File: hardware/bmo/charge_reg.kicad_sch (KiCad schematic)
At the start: 19 parts, among them U1 BQ25606RGET, U4 TPS61088RHLR

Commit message: wip start ltc4412 addition
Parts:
- added U5: LTC4412xS6, Package_TO_SOT_SMD:TSOT-23-6, symbol Power_Management:LTC4412xS6
- added U6, U7: SIA445EDJ-T1-GE3, Package_TO_SOT_SMD:Vishay_PowerPAK_SC70-6L_Single, symbol bmo:SIA445EDJ-T1-GE3

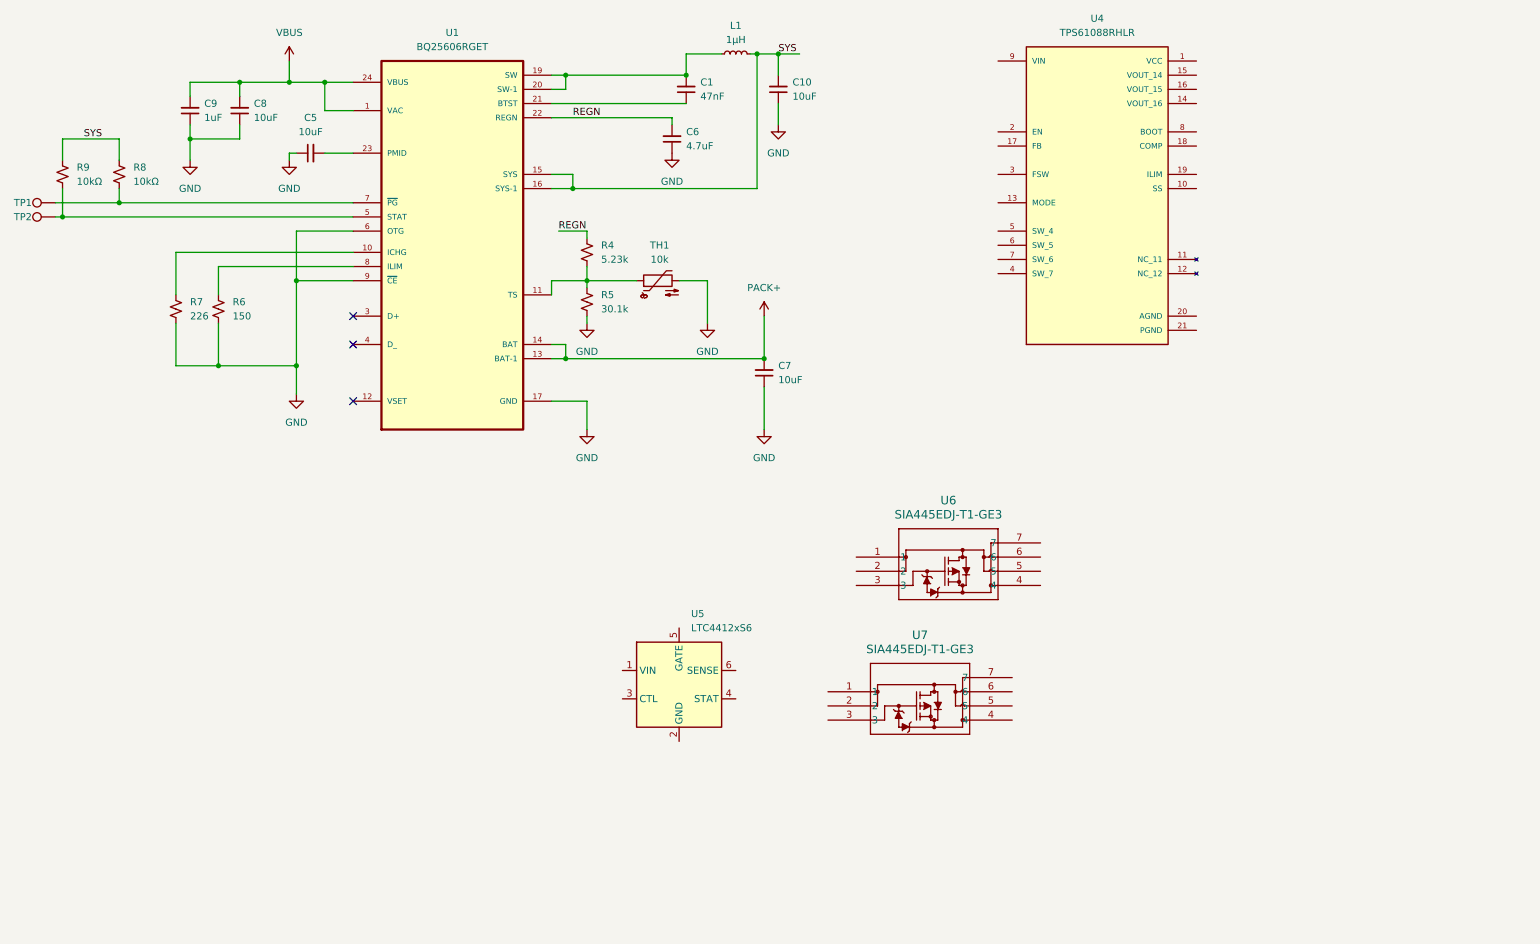
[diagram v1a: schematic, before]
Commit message: Placed and routed everything. DRC is clean.
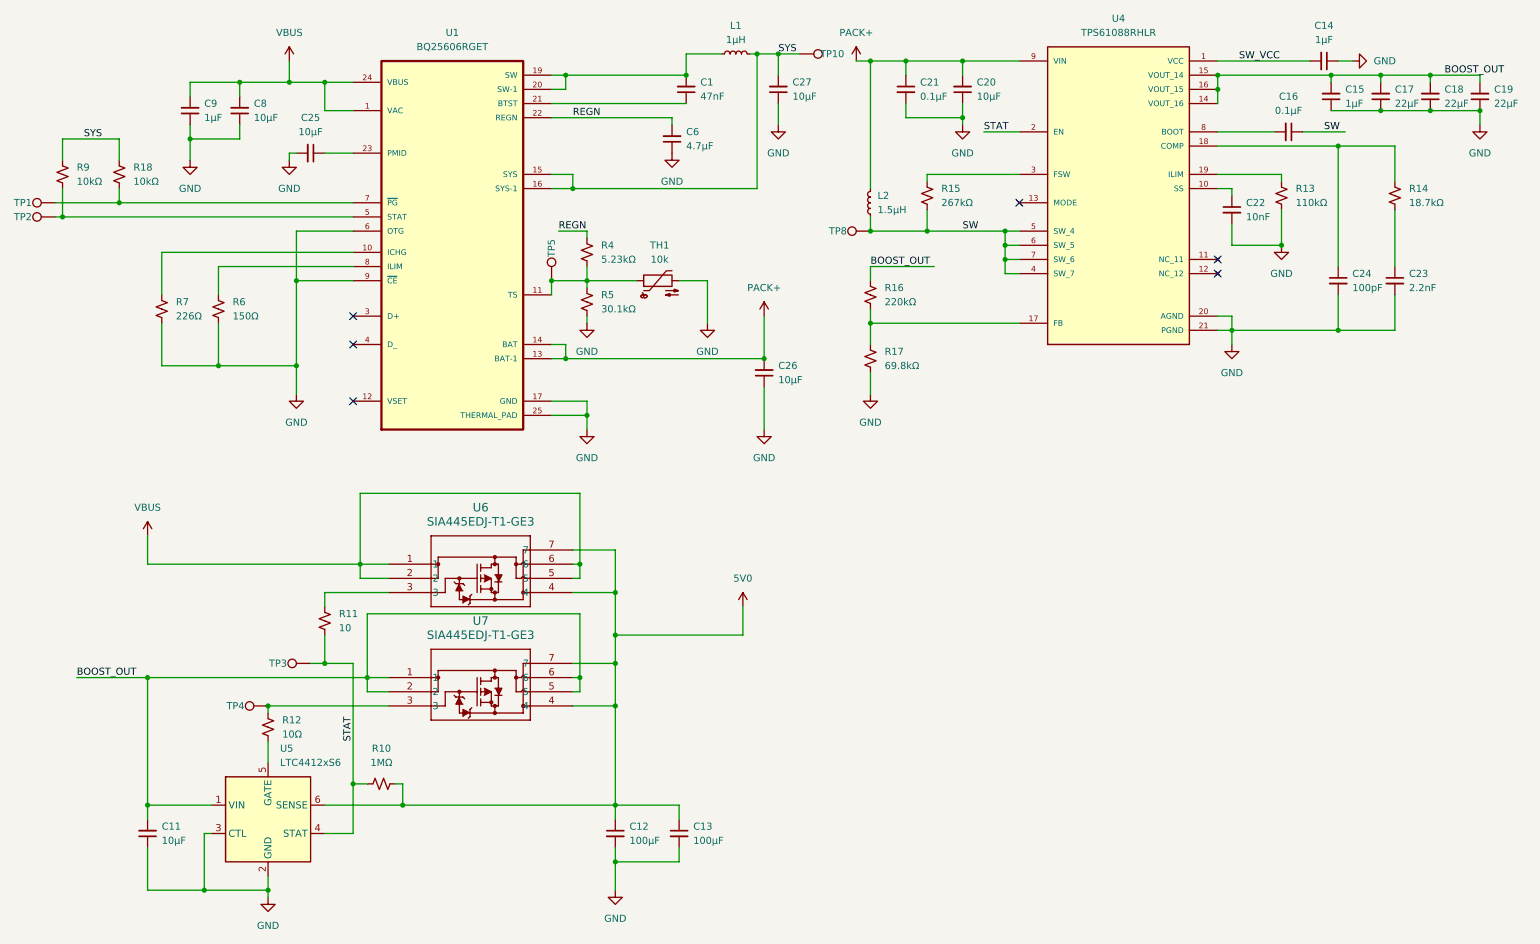
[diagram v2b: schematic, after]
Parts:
- removed C10, C5, C7: 10uF, symbol Device:C_Small
- removed R8: 10kΩ, symbol Device:R_Small_US
- added C11, C20, C25, C26, C27: 10µF, Capacitor_SMD:C_0402_1005Metric_Pad0.74x0.62mm_HandSolder, symbol Device:C_Small
- added C12, C13: 100µF, Capacitor_SMD:C_1206_3216Metric, symbol Device:C_Small
- added C14, C15: 1µF, Capacitor_SMD:C_0402_1005Metric_Pad0.74x0.62mm_HandSolder, symbol Device:C_Small
- added C16, C21: 0.1μF, Capacitor_SMD:C_0402_1005Metric_Pad0.74x0.62mm_HandSolder, symbol Device:C_Small
- added C17, C18, C19: 22µF, Capacitor_SMD:C_0603_1608Metric, symbol Device:C_Small
- added C22: 10nF, Capacitor_SMD:C_0402_1005Metric_Pad0.74x0.62mm_HandSolder, symbol Device:C_Small
- added C23: 2.2nF, Capacitor_SMD:C_0402_1005Metric_Pad0.74x0.62mm_HandSolder, symbol Device:C_Small
- added C24: 100pF, Capacitor_SMD:C_0402_1005Metric_Pad0.74x0.62mm_HandSolder, symbol Device:C_Small
- added L2: 1.5µH, bmo:74439324015, symbol Device:L_Small
- added R10: 1MΩ, Resistor_SMD:R_0402_1005Metric_Pad0.72x0.64mm_HandSolder, symbol Device:R_Small_US
- added R11: 10, Resistor_SMD:R_0402_1005Metric_Pad0.72x0.64mm_HandSolder, symbol Device:R_Small_US
- added R12: 10Ω, Resistor_SMD:R_0402_1005Metric_Pad0.72x0.64mm_HandSolder, symbol Device:R_Small_US
- added R13: 110kΩ, Resistor_SMD:R_0402_1005Metric_Pad0.72x0.64mm_HandSolder, symbol Device:R_Small_US
- added R14: 18.7kΩ, Resistor_SMD:R_0402_1005Metric_Pad0.72x0.64mm_HandSolder, symbol Device:R_Small_US
- added R15: 267kΩ, Resistor_SMD:R_0402_1005Metric_Pad0.72x0.64mm_HandSolder, symbol Device:R_Small_US
- added R16: 220kΩ, Resistor_SMD:R_0402_1005Metric_Pad0.72x0.64mm_HandSolder, symbol Device:R_Small_US
- added R17: 69.8kΩ, Resistor_SMD:R_0402_1005Metric_Pad0.72x0.64mm_HandSolder, symbol Device:R_Small_US
- added R18: 10kΩ, Resistor_SMD:R_0402_1005Metric_Pad0.72x0.64mm_HandSolder, symbol Device:R_Small_US
- added TP10, TP3, TP4, TP5, TP8: TestPoint, TestPoint:TestPoint_Pad_2.0x2.0mm, symbol Connector:TestPoint
- C1: footprint (none) -> Capacitor_SMD:C_0402_1005Metric_Pad0.74x0.62mm_HandSolder; Digikey (none) -> 490-5412-1-ND; MPN (none) -> GRM155R61A473KA01D; Manufacturer (none) -> Murata Electronics
- C6: value 4.7uF -> 4.7µF; footprint (none) -> Capacitor_SMD:C_0402_1005Metric_Pad0.74x0.62mm_HandSolder; Digikey (none) -> 1276-1482-1-ND; MPN (none) -> CL05A475MP5NRNC; Manufacturer (none) -> Samsung Electro-Mechanics
- C8: value 10uF -> 10µF; footprint (none) -> Capacitor_SMD:C_0402_1005Metric_Pad0.74x0.62mm_HandSolder; Digikey (none) -> GRM155R61A106ME11D; MPN (none) -> GRM155R61A106ME11D; Manufacturer (none) -> Murata Electronics
- C9: value 1uF -> 1µF; footprint (none) -> Capacitor_SMD:C_0402_1005Metric_Pad0.74x0.62mm_HandSolder; Digikey (none) -> 1276-1076-1-ND; MPN (none) -> CL05A105KP5NNNC; Manufacturer (none) -> Samsung Electro-Mechanics
- L1: Digikey (none) -> 541-1704-1-ND; MPN (none) -> IHLP2020ABER1R0M01; Manufacturer (none) -> Vishay Dale
- R4: value 5.23k -> 5.23kΩ; footprint (none) -> Resistor_SMD:R_0402_1005Metric_Pad0.72x0.64mm_HandSolder; Digikey (none) -> YAG3195CT-ND; MPN (none) -> RC0402FR-075K23L; Manufacturer (none) -> YAGEO
- R5: value 30.1k -> 30.1kΩ; footprint (none) -> Resistor_SMD:R_0402_1005Metric_Pad0.72x0.64mm_HandSolder; Digikey (none) -> 311-30.1KLRCT-ND; MPN (none) -> RC0402FR-0730K1L; Manufacturer (none) -> YAGEO
- R6: value 150 -> 150Ω; footprint (none) -> Resistor_SMD:R_0402_1005Metric_Pad0.72x0.64mm_HandSolder; Digikey (none) -> P150LCT-ND; MPN (none) -> ERJ-2RKF1500X; Manufacturer (none) -> Panasonic Industry
- R7: value 226 -> 226Ω; footprint (none) -> Resistor_SMD:R_0402_1005Metric_Pad0.72x0.64mm_HandSolder; Digikey (none) -> RMCF0402FT226RCT-ND; MPN (none) -> RMCF0402FT226R; Manufacturer (none) -> Stackpole Electronics Inc
- R9: footprint (none) -> Resistor_SMD:R_0402_1005Metric_Pad0.72x0.64mm_HandSolder; Digikey (none) -> RMCF0402FT10K0CT-ND; MPN (none) -> RMCF0402FT10K0; Manufacturer (none) -> Stackpole Electronics Inc
- TH1: Digikey (none) -> 4316-103AT-2-ND; MPN (none) -> 103AT-2; Manufacturer (none) -> Semitec USA Corp
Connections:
- net PGND is gone; now on net GND: U4.21 (PGND), U4.22 (PGND), U4.23 (PGND), U4.24 (PGND), U4.25 (PGND), U4.26 (PGND), U4.27 (PGND), U4.28 (PGND), U4.29 (PGND)
- net GND: now also U1.25 (THERMAL_PAD), U4.20 (AGND), U5.2 (GND), U5.3 (CTL), C11.1, C12.2, C13.2, C14.1, C15.1, C17.1, C18.1, C19.1, C20.1, C21.2, C22.2, C23.2, C24.2, C25.2, C26.1, C27.1, R13.1, R17.2
- net PACK+: now also U4.9 (VIN), C20.2, C21.1, C26.2, L2.2
- net SYS: now also C27.2, R18.1, TP10.1
- net VBUS: now also U6.1, U6.2, U6.5, U6.6
- net at R4.2, R5.1, TH1.1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: now also TP5.1
- net at TP1.1, U1.7 (~{PG}): now also R18.2
- net BOOST_OUT: now reaches U7.1
- net BOOST_OUT: now also U4.14 (VOUT_16), U4.15 (VOUT_14), U4.16 (VOUT_15), U5.1 (VIN), U7.2, U7.5, U7.6, C11.2, C15.2, C17.2, C18.2, C19.2, R16.1
- net at U7.3: now also R12.1, TP4.1
- net 5V0: now reaches U7.4
- net 5V0: now also U5.6 (SENSE), U6.4, U6.7, U7.7, C12.1, C13.1, R10.2
- net at U1.23 (PMID): now also C25.1
- net STAT: now reaches U5.4 (STAT)
- net STAT: now also U4.2 (EN), R10.1, R11.2, TP3.1
- net at U5.5 (GATE): now also R12.2
- net SW_VCC: now reaches U4.1 (VCC)
- net SW_VCC: now also C14.2
- net at U4.10 (SS): now also C22.1
- net at U4.17 (FB): now also R16.2, R17.1
- net at U4.18 (COMP): now also C24.1, R14.2
- net at U4.19 (ILIM): now also R13.2
- net at U4.3 (FSW): now also R15.1
- net SW: now reaches U4.4 (SW_7)
- net SW: now also U4.5 (SW_4), U4.6 (SW_5), U4.7 (SW_6), C16.1, L2.1, R15.2, TP8.1
- net at U4.8 (BOOT): now also C16.2
- net at U6.3: now also R11.1
- new net: C23.1, R14.1
- no-connect marks 3 -> 6
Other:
- moved on the sheet: R7, U4, U5, U6, U7
